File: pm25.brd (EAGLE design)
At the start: 55.9 x 33 mm, 36 parts, among them J1 CON-0024, Q1 TRANSISTOR-NPN-40V-0.2A-SOT23, Q2 TR-0001, U1 POWER-VREG-FB-EN-SW-350MA, U2 CCS811B-JOPD500, U3 POWER-SWITCH-SIP32509DT, U4 SI7021-A20-GM1R

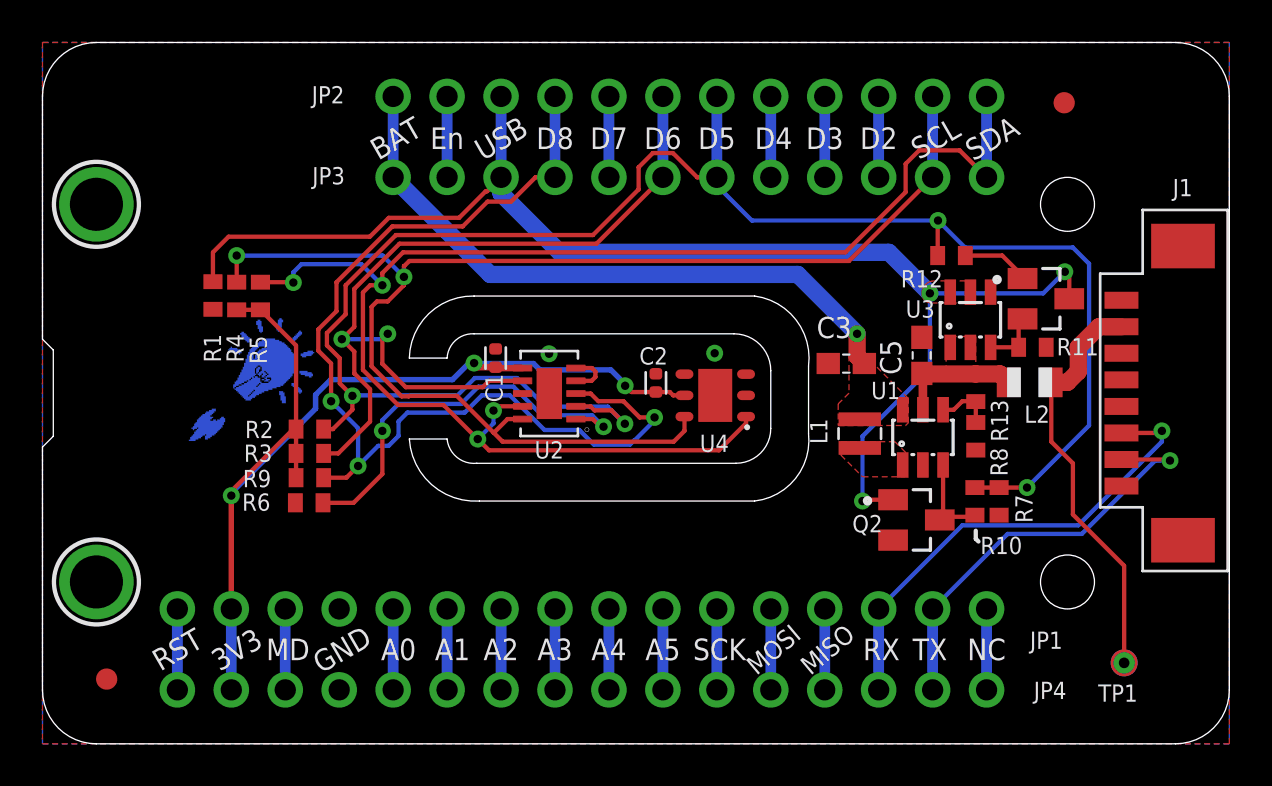
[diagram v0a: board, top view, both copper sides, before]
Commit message: remove dust sensor and other extra circuitry
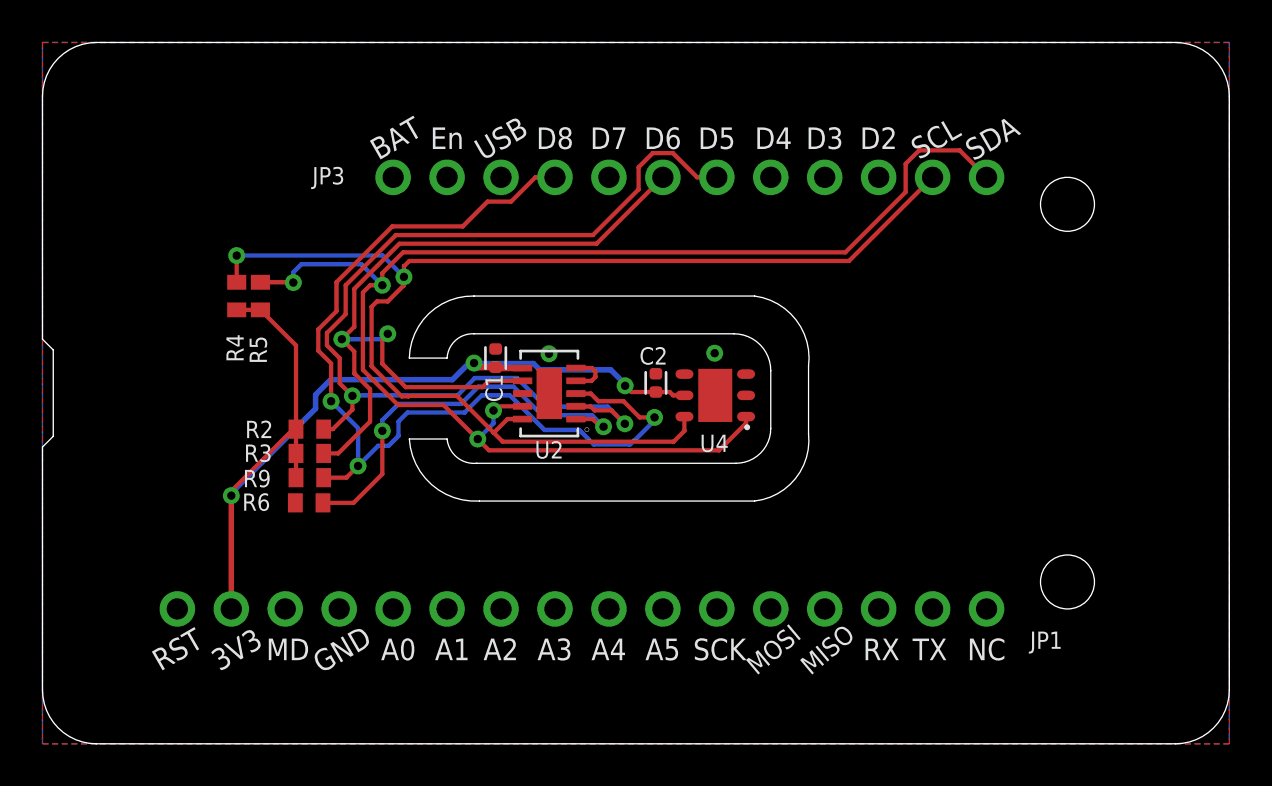
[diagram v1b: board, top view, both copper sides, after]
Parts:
- removed C3: 4.7u, wolff-den:C0603
- removed C5: 10u, wolff-den:C0603
- removed J1: CON-0024, wolff-den:0532610871
- removed JP2: (no value), microbuilder:1X12_ROUND
- removed JP4: (no value), microbuilder:1X16_ROUND
- removed L1: 4.7u, wolff-den:IND-2P0X2P0X1P2
- removed L2: 2k, wolff-den:R0805
- removed PCB1: PCB-PS-CCS811-SI7021, wolff-den:PLACEHOLDER
- removed Q1: TRANSISTOR-NPN-40V-0.2A-SOT23, wolff-den:SOT23
- removed Q2: TR-0001, wolff-den:SOT23
- removed R1, R10, R11, R7: 100k, wolff-den:R0402
- removed R12: 1k, wolff-den:R0402
- removed R13: 976k, wolff-den:R0402
- removed R8: 309k, wolff-den:R0402
- removed TP1: TP, wolff-den:TP-1P27
- removed U$31, U$32: MOUNTINGHOLE2.5, microbuilder:MOUNTINGHOLE_2.5_PLATED
- removed U$34, U$35: FIDUCIAL"", microbuilder:FIDUCIAL_1MM
- removed U1: POWER-VREG-FB-EN-SW-350MA, wolff-den:SOT23-6
- removed U3: POWER-SWITCH-SIP32509DT, wolff-den:SOT23-6
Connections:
- removed net N$1: L1.P$1, U1.1
- removed net N$2: R13.1, R8.2, U1.4
- removed net N$3: Q1.2, R11.2, U3.3
- removed net N$6: Q2.3, R10.1, U1.3
- removed net N$7: Q1.1, R12.2
- removed net V5V0_BEAD: C5.1, L2.1, R13.2, U1.5, U3.1, U3.2
- removed net V5V0_HAT: J1.2, L2.2, TP1.P$1, TP1.P$2, TP1.TP
- net !RESET: no longer JP4.16
- net +3V3: no longer JP4.15
- net A0: no longer JP4.12
- net A1: no longer JP4.11
- net A2: no longer JP4.10
- net A3: no longer JP4.9
- net A4: no longer JP4.8
- net A5: no longer JP4.7
- net D2: no longer JP2.10
- net D3: no longer JP2.9
- net D4: no longer JP2.8
- net D5: no longer JP2.7, R10.2, R12.1, R7.2
- net D6: no longer JP2.6
- net D7: no longer JP2.5
- net D8: no longer JP2.4
- net EN: no longer JP2.2
- net GND: no longer C3.2, C5.2, J1.8, JP4.13, Q2.2, R1.1, R11.1, R7.1, R8.1, U1.2, U3.4
- net MD: no longer JP4.14
- net MISO: no longer JP4.4
- net MOSI: no longer JP4.5
- net NC: no longer JP4.1
- net RX: no longer J1.6, JP4.3
- net SCK: no longer JP4.6
- net SCL: no longer JP2.11
- net SDA: no longer JP2.12
- net TX: no longer J1.7, JP4.2
- net VBAT: no longer C3.1, JP2.1, L1.P$2, U1.6
- net VBUS: no longer JP2.3, Q1.3, Q2.1, R1.2, U3.5, U3.6
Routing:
- net VBUS: track 64.0 -> 0.00 mm, vias 3 -> 0
- net D5: track 85.4 -> 46.3 mm, vias 4 -> 2
- net VBAT: track 30.2 -> 0.00 mm, vias 1 -> 0
- net RX: track 22.9 -> 0.00 mm, vias 1 -> 0
- net TX: track 20.3 -> 0.00 mm, vias 1 -> 0
- net V5V0_HAT: track 19.7 -> 0.00 mm
- net V5V0_BEAD: track 5.94 -> 0.00 mm
- net N$6: track 4.18 -> 0.00 mm
- net SCL: track 64.4 -> 60.6 mm
- net D8: track 49.4 -> 45.6 mm
- net +3V3: track 50.8 -> 47.0 mm
- net SCK: track 3.81 -> 0.00 mm
- net NC: track 3.81 -> 0.00 mm
- net MOSI: track 3.81 -> 0.00 mm
- net MISO: track 3.81 -> 0.00 mm
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- removed copper zone on layer 1, net N$1
- removed copper zone on layer 1, net V5V0_BEAD
- removed copper zone on layer 1, net VBAT
- removed copper zone on layer 1, net VBUS
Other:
- board text removed: ">LAST_DATE_TIME"

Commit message: made a cut out that extends to a smaller board size
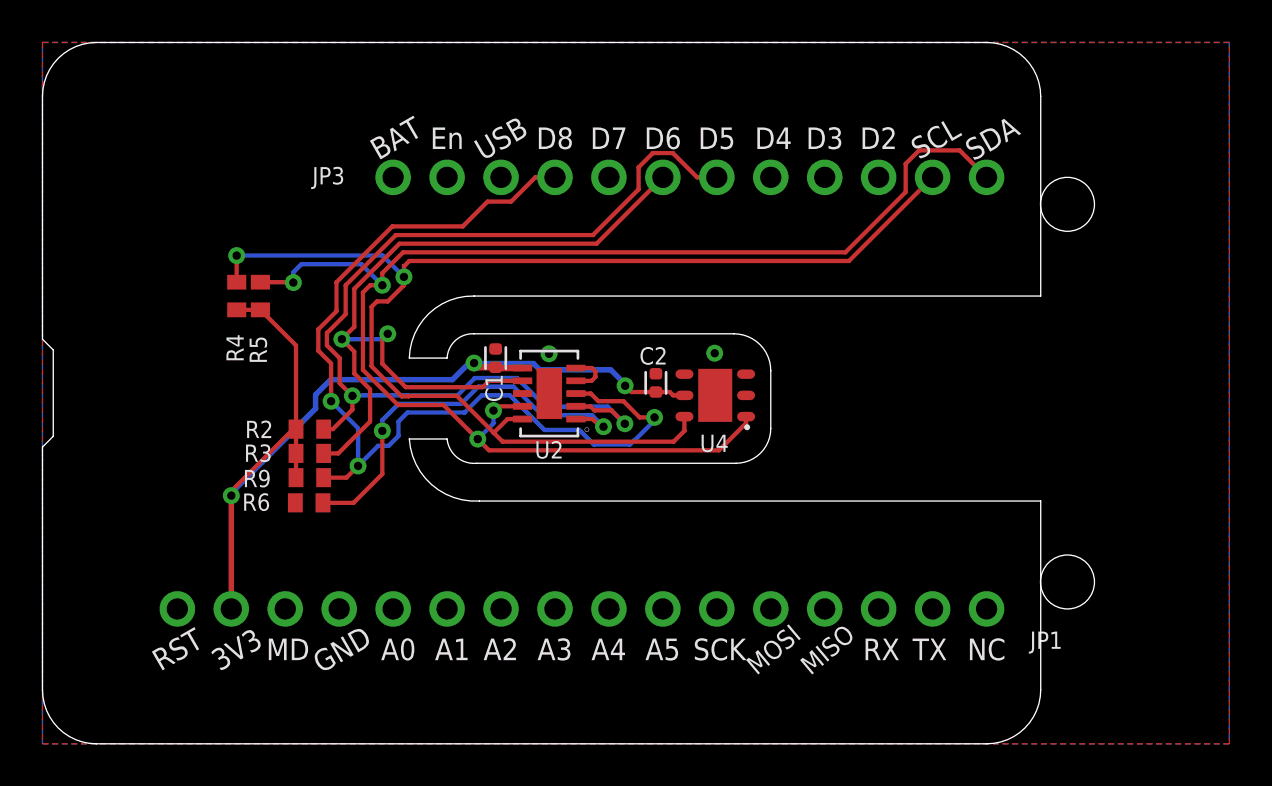
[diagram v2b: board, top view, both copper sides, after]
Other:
- board size 55.9 x 33 mm -> 47 x 33 mm
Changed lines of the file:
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@@
 <layer number="20" name="Dimension" color="15" fill="1" visible="yes" active="yes"/>
 <layer number="21" name="tPlace" color="14" fill="1" visible="yes" active="yes"/>
-<layer number="22" name="bPlace" color="14" fill="1" visible="no" active="yes"/>
+<layer number="22" name="bPlace" color="14" fill="1" visible="yes" active="yes"/>
 <layer number="23" name="tOrigins" color="14" fill="1" visible="yes" active="yes"/>
-<layer number="24" name="bOrigins" color="13" fill="1" visible="no" active="yes"/>
+<layer number="24" name="bOrigins" color="13" fill="1" visible="yes" active="yes"/>
 <layer number="25" name="tNames" color="7" fill="1" visible="yes" active="yes"/>
-<layer number="26" name="bNames" color="7" fill="1" visible="no" active="yes"/>
+<layer number="26" name="bNames" color="7" fill="1" visible="yes" active="yes"/>
 <layer number="27" name="tValues" color="7" fill="1" visible="no" active="yes"/>
 <layer number="28" name="bValues" color="7" fill="1" visible="no" active="yes"/>
@@
 <layer number="38" name="bTest" color="7" fill="1" visible="no" active="yes"/>
 <layer number="39" name="tKeepout" color="4" fill="11" visible="yes" active="yes"/>
-<layer number="40" name="bKeepout" color="1" fill="11" visible="no" active="yes"/>
+<layer number="40" name="bKeepout" color="1" fill="11" visible="yes" active="yes"/>
 <layer number="41" name="tRestrict" color="4" fill="10" visible="yes" active="yes"/>
-<layer number="42" name="bRestrict" color="1" fill="10" visible="no" active="yes"/>
+<layer number="42" name="bRestrict" color="1" fill="10" visible="yes" active="yes"/>
 <layer number="43" name="vRestrict" color="2" fill="10" visible="no" active="yes"/>
 <layer number="44" name="Drills" color="7" fill="1" visible="no" active="yes"/>
@@
 <layer number="50" name="dxf" color="7" fill="1" visible="no" active="no"/>
 <layer number="51" name="tDocu" color="7" fill="1" visible="yes" active="yes"/>
-<layer number="52" name="bDocu" color="7" fill="1" visible="no" active="yes"/>
+<layer number="52" name="bDocu" color="7" fill="1" visible="yes" active="yes"/>
 <layer number="53" name="tGND_GNDA" color="7" fill="9" visible="no" active="no"/>
 <layer number="54" name="bGND_GNDA" color="1" fill="9" visible="no" active="no"/>
@@
 <fusionsync huburn="a.cGVyc29uYWw6dWUyZDcxOWFm" projecturn="a.cGVyc29uYWw6dWUyZDcxOWFmIzIwMTkwMzIxMTgzNjY2NTgx" f3durn="urn:adsk.wipprod:dm.lineage:of-WC7iUTR6j-QJaXZ4WSA" pcbguid="2ada34ed-02e3-4764-ae65-c304e2d58fe2" lastpulledtime="" lastsyncedchangeguid="c324f360-4e1b-41e3-ea26-84c460706219"/>
 <plain>
-<wire x1="2.54" y1="0" x2="53.34" y2="0" width="0" layer="20"/>
-<wire x1="53.34" y1="0" x2="55.88" y2="2.54" width="0" layer="20" curve="90"/>
-<wire x1="55.88" y1="2.54" x2="55.88" y2="30.48" width="0" layer="20"/>
-<wire x1="55.88" y1="30.48" x2="53.34" y2="33.02" width="0" layer="20" curve="90"/>
-<wire x1="53.34" y1="33.02" x2="2.54" y2="33.02" width="0" layer="20"/>
+<wire x1="2.54" y1="0" x2="44.46" y2="0" width="0" layer="20"/>
+<wire x1="44.46" y1="0" x2="47" y2="2.54" width="0" layer="20" curve="90"/>
+<wire x1="47" y1="2.54" x2="47" y2="11.43" width="0" layer="20"/>
+<wire x1="47" y1="21.082" x2="47" y2="30.48" width="0" layer="20"/>
+<wire x1="47" y1="30.48" x2="44.46" y2="33.02" width="0" layer="20" curve="90"/>
+<wire x1="44.46" y1="33.02" x2="2.54" y2="33.02" width="0" layer="20"/>
 <wire x1="2.54" y1="33.02" x2="0" y2="30.48" width="0" layer="20" curve="90"/>
 <wire x1="0" y1="30.48" x2="0" y2="19.05" width="0" layer="20"/>
@@
 <rectangle x1="46.41341875" y1="17.50695" x2="46.85538125" y2="17.57045" layer="22" rot="R180"/>
 <rectangle x1="40.63238125" y1="17.50695" x2="41.01591875" y2="17.57045" layer="22" rot="R180"/>
-<wire x1="33.528" y1="11.43" x2="20.574" y2="11.43" width="0" layer="20"/>
+<wire x1="47" y1="11.43" x2="20.574" y2="11.43" width="0" layer="20"/>
 <wire x1="20.574" y1="11.43" x2="17.272" y2="14.351" width="0" layer="20" curve="-90"/>
-<wire x1="33.528" y1="11.43" x2="36.068" y2="14.605" width="0" layer="20" curve="90"/>
-<wire x1="36.068" y1="14.605" x2="36.068" y2="17.78" width="0" layer="20"/>
-<wire x1="36.068" y1="17.78" x2="33.528" y2="21.082" width="0" layer="20" curve="90"/>
-<wire x1="33.528" y1="21.082" x2="20.32" y2="21.082" width="0" layer="20"/>
+<wire x1="47" y1="21.082" x2="20.32" y2="21.082" width="0" layer="20"/>
 <wire x1="20.32" y1="21.082" x2="17.272" y2="18.161" width="0" layer="20" curve="90"/>
 <wire x1="17.272" y1="18.161" x2="19.05" y2="18.161" width="0" layer="20"/>
